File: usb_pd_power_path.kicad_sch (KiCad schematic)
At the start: 79 parts, among them Q10 Q_PMOS_DGS, Q11 Q_NMOS_DGS, Q12 Q_NMOS_DGS, Q13 Q_NMOS_DGS, Q14 Q_NMOS_DGS, Q15 Q_PMOS_DGS, Q16 Q_PMOS_DGS, Q17 Q_NMOS_DGS, Q18 Q_NMOS_DGS, Q9 Q_PMOS_DGS, U15 LM358, U16 MP2229GQ-P, U17 MP2229GQ-P

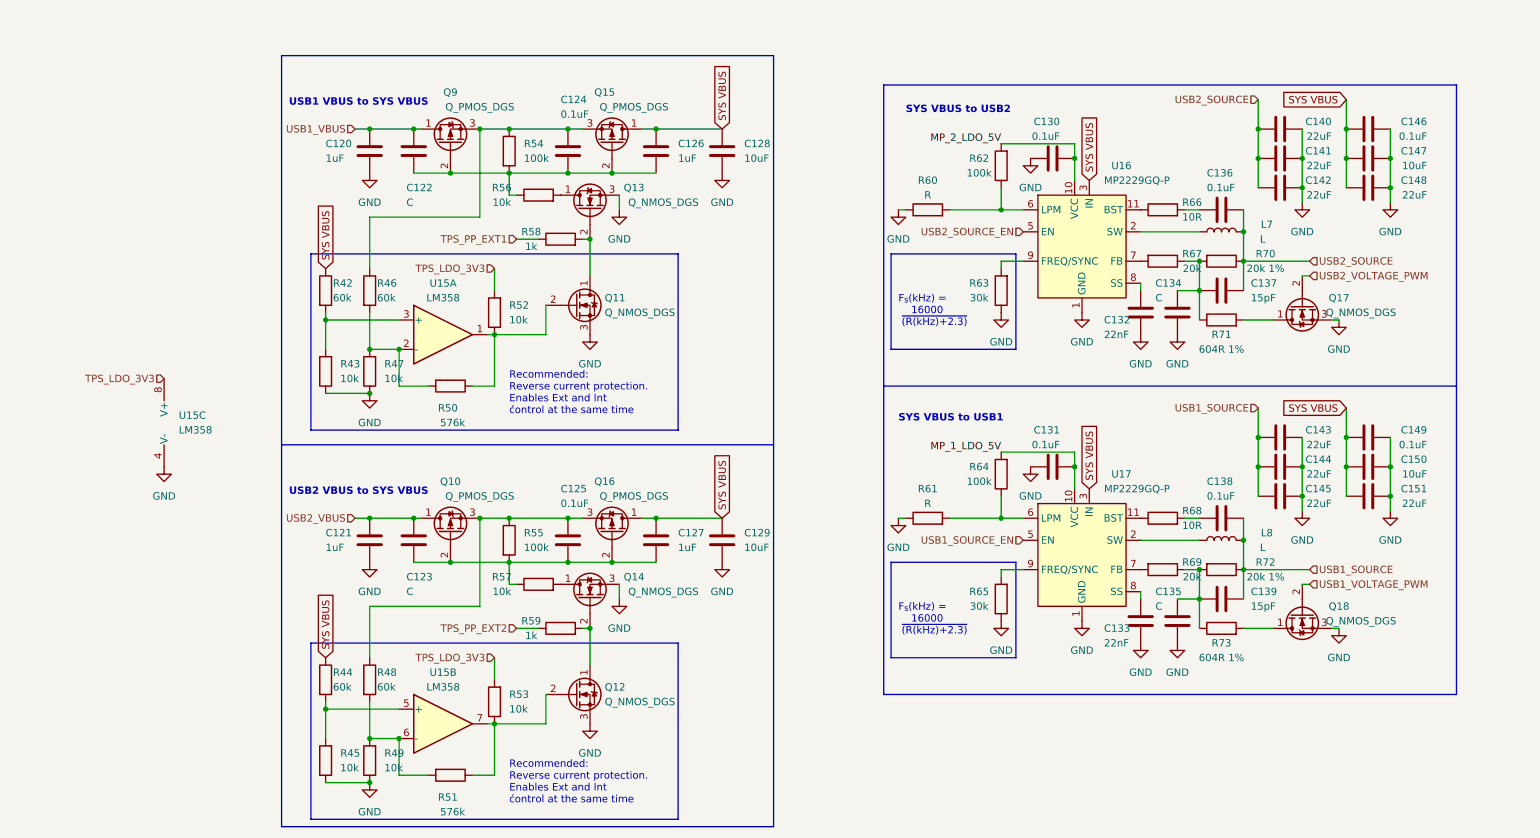
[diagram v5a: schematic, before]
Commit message: added nfc antenna components, added most of footprints
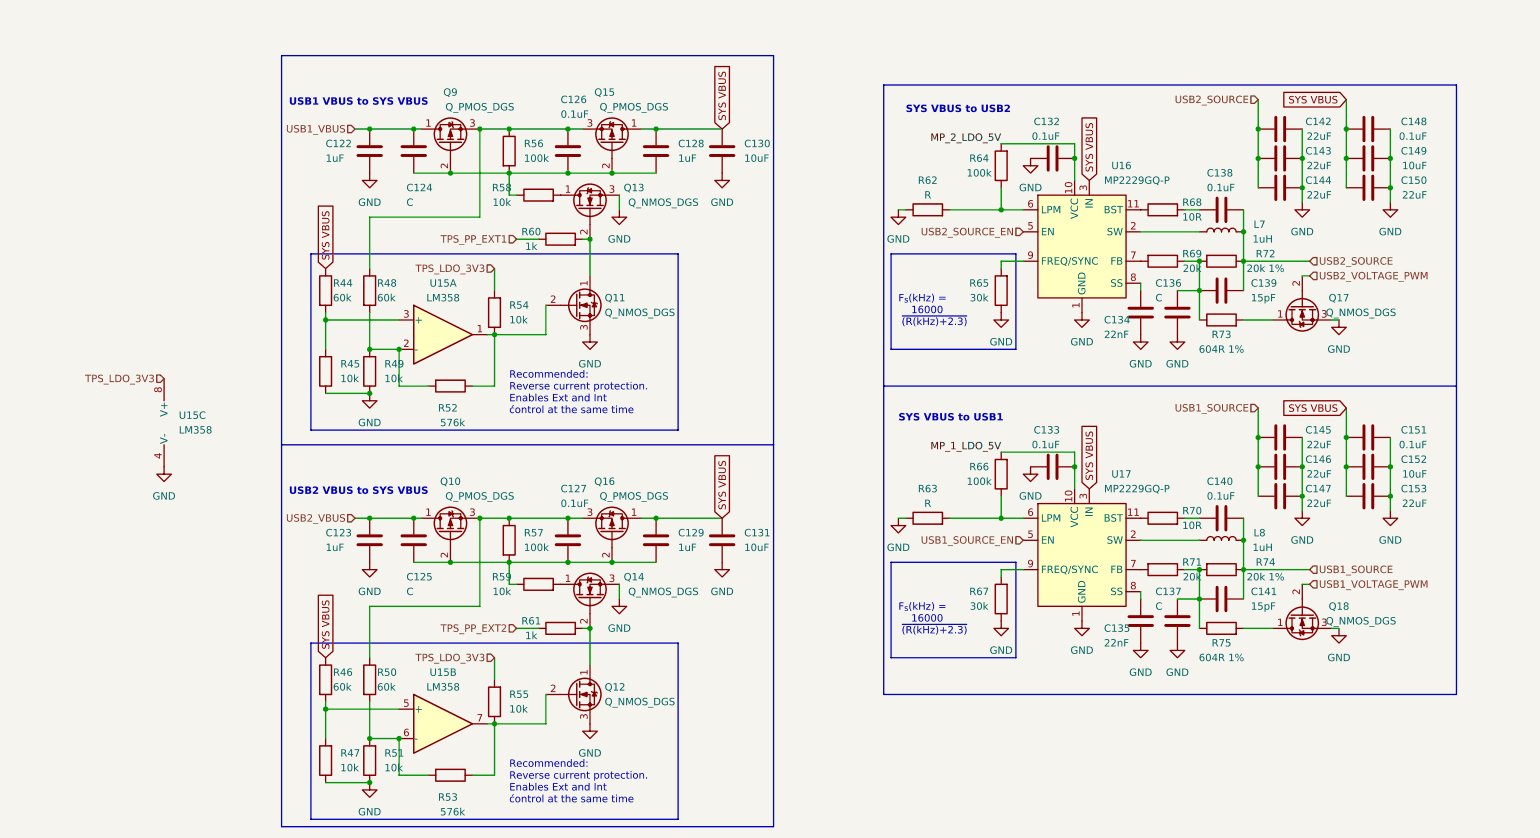
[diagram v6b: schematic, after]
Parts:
- C122: renamed from C120; footprint (none) -> Capacitor_SMD:C_0603_1608Metric_Pad1.08x0.95mm_HandSolder
- C123: renamed from C121; footprint (none) -> Capacitor_SMD:C_0603_1608Metric_Pad1.08x0.95mm_HandSolder
- C124: renamed from C122; footprint (none) -> Capacitor_SMD:C_0603_1608Metric_Pad1.08x0.95mm_HandSolder
- C125: renamed from C123; footprint (none) -> Capacitor_SMD:C_0603_1608Metric_Pad1.08x0.95mm_HandSolder
- C126: renamed from C124; footprint (none) -> Capacitor_SMD:C_0603_1608Metric_Pad1.08x0.95mm_HandSolder
- C127: renamed from C125; footprint (none) -> Capacitor_SMD:C_0603_1608Metric_Pad1.08x0.95mm_HandSolder
- C128: renamed from C126; footprint (none) -> Capacitor_SMD:C_0603_1608Metric_Pad1.08x0.95mm_HandSolder
- C129: renamed from C127; footprint (none) -> Capacitor_SMD:C_0603_1608Metric_Pad1.08x0.95mm_HandSolder
- C132: renamed from C130; footprint (none) -> Capacitor_SMD:C_0603_1608Metric_Pad1.08x0.95mm_HandSolder
- C133: renamed from C131; footprint (none) -> Capacitor_SMD:C_0603_1608Metric_Pad1.08x0.95mm_HandSolder
- C134: renamed from C132; footprint (none) -> Capacitor_SMD:C_0603_1608Metric_Pad1.08x0.95mm_HandSolder
- C135: renamed from C133; footprint (none) -> Capacitor_SMD:C_0603_1608Metric_Pad1.08x0.95mm_HandSolder
- C136: renamed from C134; footprint (none) -> Capacitor_SMD:C_0603_1608Metric_Pad1.08x0.95mm_HandSolder
- C137: renamed from C135; footprint (none) -> Capacitor_SMD:C_0603_1608Metric_Pad1.08x0.95mm_HandSolder
- C138: renamed from C136; footprint (none) -> Capacitor_SMD:C_0603_1608Metric_Pad1.08x0.95mm_HandSolder
- C139: renamed from C137; footprint (none) -> Capacitor_SMD:C_0603_1608Metric_Pad1.08x0.95mm_HandSolder
- C140: renamed from C138; footprint (none) -> Capacitor_SMD:C_0603_1608Metric_Pad1.08x0.95mm_HandSolder
- C141: renamed from C139; footprint (none) -> Capacitor_SMD:C_0603_1608Metric_Pad1.08x0.95mm_HandSolder
- C148: renamed from C146; footprint (none) -> Capacitor_SMD:C_0603_1608Metric_Pad1.08x0.95mm_HandSolder
- C151: renamed from C149; footprint (none) -> Capacitor_SMD:C_0603_1608Metric_Pad1.08x0.95mm_HandSolder
- L7, L8: value L -> 1uH
- R44: renamed from R42; footprint (none) -> Resistor_SMD:R_0603_1608Metric_Pad0.98x0.95mm_HandSolder
- R45: renamed from R43; footprint (none) -> Resistor_SMD:R_0603_1608Metric_Pad0.98x0.95mm_HandSolder
- R46: renamed from R44; footprint (none) -> Resistor_SMD:R_0603_1608Metric_Pad0.98x0.95mm_HandSolder
- R47: renamed from R45; footprint (none) -> Resistor_SMD:R_0603_1608Metric_Pad0.98x0.95mm_HandSolder
- R48: renamed from R46; footprint (none) -> Resistor_SMD:R_0603_1608Metric_Pad0.98x0.95mm_HandSolder
- R49: renamed from R47; footprint (none) -> Resistor_SMD:R_0603_1608Metric_Pad0.98x0.95mm_HandSolder
- R50: renamed from R48; footprint (none) -> Resistor_SMD:R_0603_1608Metric_Pad0.98x0.95mm_HandSolder
- R51: renamed from R49; footprint (none) -> Resistor_SMD:R_0603_1608Metric_Pad0.98x0.95mm_HandSolder
- R52: renamed from R50; footprint (none) -> Resistor_SMD:R_0603_1608Metric_Pad0.98x0.95mm_HandSolder
- R53: renamed from R51; footprint (none) -> Resistor_SMD:R_0603_1608Metric_Pad0.98x0.95mm_HandSolder
- R54: renamed from R52; footprint (none) -> Resistor_SMD:R_0603_1608Metric_Pad0.98x0.95mm_HandSolder
- R55: renamed from R53; footprint (none) -> Resistor_SMD:R_0603_1608Metric_Pad0.98x0.95mm_HandSolder
- R56: renamed from R54; footprint (none) -> Resistor_SMD:R_0603_1608Metric_Pad0.98x0.95mm_HandSolder
- R57: renamed from R55; footprint (none) -> Resistor_SMD:R_0603_1608Metric_Pad0.98x0.95mm_HandSolder
- R58: renamed from R56; footprint (none) -> Resistor_SMD:R_0603_1608Metric_Pad0.98x0.95mm_HandSolder
- R59: renamed from R57; footprint (none) -> Resistor_SMD:R_0603_1608Metric_Pad0.98x0.95mm_HandSolder
- R60: renamed from R58; footprint (none) -> Resistor_SMD:R_0603_1608Metric_Pad0.98x0.95mm_HandSolder
- R61: renamed from R59; footprint (none) -> Resistor_SMD:R_0603_1608Metric_Pad0.98x0.95mm_HandSolder
- R62: renamed from R60; footprint (none) -> Resistor_SMD:R_0603_1608Metric_Pad0.98x0.95mm_HandSolder
- R63: renamed from R61; footprint (none) -> Resistor_SMD:R_0603_1608Metric_Pad0.98x0.95mm_HandSolder
- R64: renamed from R62; footprint (none) -> Resistor_SMD:R_0603_1608Metric_Pad0.98x0.95mm_HandSolder
- R65: renamed from R63; footprint (none) -> Resistor_SMD:R_0603_1608Metric_Pad0.98x0.95mm_HandSolder
- R66: renamed from R64; footprint (none) -> Resistor_SMD:R_0603_1608Metric_Pad0.98x0.95mm_HandSolder
- R67: renamed from R65; footprint (none) -> Resistor_SMD:R_0603_1608Metric_Pad0.98x0.95mm_HandSolder
- R68: renamed from R66; footprint (none) -> Resistor_SMD:R_0603_1608Metric_Pad0.98x0.95mm_HandSolder
- R69: renamed from R67; footprint (none) -> Resistor_SMD:R_0603_1608Metric_Pad0.98x0.95mm_HandSolder
- R70: renamed from R68; footprint (none) -> Resistor_SMD:R_0603_1608Metric_Pad0.98x0.95mm_HandSolder
- R71: renamed from R69; footprint (none) -> Resistor_SMD:R_0603_1608Metric_Pad0.98x0.95mm_HandSolder
- R72: renamed from R70; footprint (none) -> Resistor_SMD:R_0603_1608Metric_Pad0.98x0.95mm_HandSolder
- R73: renamed from R71; footprint (none) -> Resistor_SMD:R_0603_1608Metric_Pad0.98x0.95mm_HandSolder
- R74: renamed from R72; footprint (none) -> Resistor_SMD:R_0603_1608Metric_Pad0.98x0.95mm_HandSolder
- R75: renamed from R73; footprint (none) -> Resistor_SMD:R_0603_1608Metric_Pad0.98x0.95mm_HandSolder
- U15: footprint (none) -> Package_SO:SOIC-8_3.9x4.9mm_P1.27mm
- U16, U17: footprint (none) -> airsoft_controller:QFN-14
- renumbered C128 to C130, C129 to C131, C140 to C142, C141 to C143, C142 to C144, C143 to C145, C144 to C146, C145 to C147, C147 to C149, C148 to C150, C150 to C152, C151 to C153

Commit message: schematic creation
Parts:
- removed Q10, Q15, Q16, Q9: Q_PMOS_DGS, symbol Device:Q_PMOS_DGS
- added Q10, Q9: Q_Dual_PMOS, Package_SO:SO-8_3.9x4.9mm_P1.27mm, symbol Device:Q_Dual_PMOS_S1G1S2G2D2D2D1D1
- added R63, R64: 100k, Resistor_SMD:R_0603_1608Metric_Pad0.98x0.95mm_HandSolder, symbol Device:R
- C132: renamed from C124; value C -> 0.1uF
- C133: renamed from C125; value C -> 0.1uF
- C136: renamed from C128; value 1uF -> 0.1uF
- C137: renamed from C129; value 1uF -> 0.1uF
- C138: renamed from C130; footprint (none) -> Capacitor_SMD:C_0805_2012Metric_Pad1.18x1.45mm_HandSolder
- C139: renamed from C131; footprint (none) -> Capacitor_SMD:C_0805_2012Metric_Pad1.18x1.45mm_HandSolder
- C150: renamed from C142; footprint (none) -> Capacitor_SMD:CP_Elec_5x5.3; symbol Device:C -> Device:C_Polarized
- C151: renamed from C143; footprint (none) -> Capacitor_SMD:CP_Elec_5x5.3; symbol Device:C -> Device:C_Polarized
- C152: renamed from C144; footprint (none) -> Capacitor_SMD:CP_Elec_5x5.3; symbol Device:C -> Device:C_Polarized
- C153: renamed from C145; footprint (none) -> Capacitor_SMD:CP_Elec_5x5.3; symbol Device:C -> Device:C_Polarized
- C154: renamed from C146; footprint (none) -> Capacitor_SMD:CP_Elec_5x5.3; symbol Device:C -> Device:C_Polarized
- C155: renamed from C147; footprint (none) -> Capacitor_SMD:CP_Elec_5x5.3; symbol Device:C -> Device:C_Polarized
- C157: renamed from C149; footprint (none) -> Capacitor_SMD:C_1206_3216Metric_Pad1.33x1.80mm_HandSolder
- C158: renamed from C150; footprint (none) -> Capacitor_SMD:CP_Elec_5x5.3; symbol Device:C -> Device:C_Polarized
- C160: renamed from C152; footprint (none) -> Capacitor_SMD:C_1206_3216Metric_Pad1.33x1.80mm_HandSolder
- C161: renamed from C153; footprint (none) -> Capacitor_SMD:CP_Elec_5x5.3; symbol Device:C -> Device:C_Polarized
- L7, L8: footprint (none) -> airsoft_controller:Inductor_8030
- Q11, Q12, Q13, Q14: footprint (none) -> Package_TO_SOT_SMD:SOT-23; symbol Device:Q_NMOS_DGS -> Device:Q_NMOS_GSD
- Q15: renamed from Q17; footprint (none) -> Package_TO_SOT_SMD:SOT-23; symbol Device:Q_NMOS_DGS -> Device:Q_NMOS_GSD
- Q16: renamed from Q18; footprint (none) -> Package_TO_SOT_SMD:SOT-23; symbol Device:Q_NMOS_DGS -> Device:Q_NMOS_GSD
- renumbered C122 to C130, C123 to C131, C126 to C134, C127 to C135, C132 to C140, C133 to C141, C134 to C142, C135 to C143, C136 to C144, C137 to C145, C138 to C146, C139 to C147, C140 to C148, C141 to C149, C148 to C156, C151 to C159, R44 to R45, R45 to R46, R46 to R47, R47 to R48, R48 to R49, R49 to R50, R50 to R51, R51 to R52, R52 to R53, R53 to R54, R54 to R55, R55 to R56, R56 to R57, R57 to R58, R58 to R59, R59 to R60, R60 to R61, R61 to R62, R62 to R65, R63 to R66, R64 to R67, R65 to R68, R66 to R69, R67 to R70, R68 to R71, R69 to R72, R70 to R73, R71 to R74, R72 to R75, R73 to R76, R74 to R77, R75 to R78, U15 to U17, U16 to U18, U17 to U19
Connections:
- net GND: now also Q11.2 (S), Q12.2 (S), Q13.2 (S), Q14.2 (S), Q15.2 (S), Q16.2 (S), R63.2, R64.2; no longer Q11.3 (S), Q12.3 (S), Q13.3 (S), Q14.3 (S), Q15.3 (S), Q16.3 (S)
- net SYS VBUS: now also U18.15 (IN), U19.15 (IN), Q10.5 (D), Q10.6 (G), Q9.5 (D), Q9.6 (G); no longer U18.PAD (IN), U19.PAD (IN)
- net USB1_VBUS: now also Q9.7 (D), Q9.8 (G)
- net USB1_VOLTAGE_PWM: now also Q16.1 (G); no longer Q16.2 (G)
- net USB2_VBUS: now also Q10.7 (D), Q10.8 (G)
- net USB2_VOLTAGE_PWM: now also Q15.1 (G); no longer Q15.2 (G)
- net at R76.2: now also Q15.3 (D); no longer Q15.1 (D)
- net at C133.2, C135.2, C137.2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: now also Q10.2 (G), Q10.4 (G)
- net at R53.1, R55.1, U17.1: now also Q11.1 (G); no longer Q11.2 (G)
- net at R60.2: now also Q14.3 (D); no longer Q14.1 (D)
- net at C132.2, C134.2, C136.2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: now also Q9.2 (G), Q9.4 (G)
- net at Q13.1 (G): now also Q11.3 (D), R61.2, R63.1; no longer R59.2
- net at C134.1, R49.1, R57.1: now also Q9.1 (S), Q9.3 (S)
- net at C135.1, R51.1, R58.1: now also Q10.1 (S), Q10.3 (S)
- net at R54.1, R56.1, U17.7: now also Q12.1 (G); no longer Q12.2 (G)
- net at R78.2: now also Q16.3 (D); no longer Q16.1 (D)
- new net: Q13.3 (D), R59.2
- new net: Q12.3 (D), Q14.1 (G), R62.2, R64.1
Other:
- moved on the sheet: C141, C143, C145, C148, C149, C159, C160, L8, Q15, Q16, R66, R69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

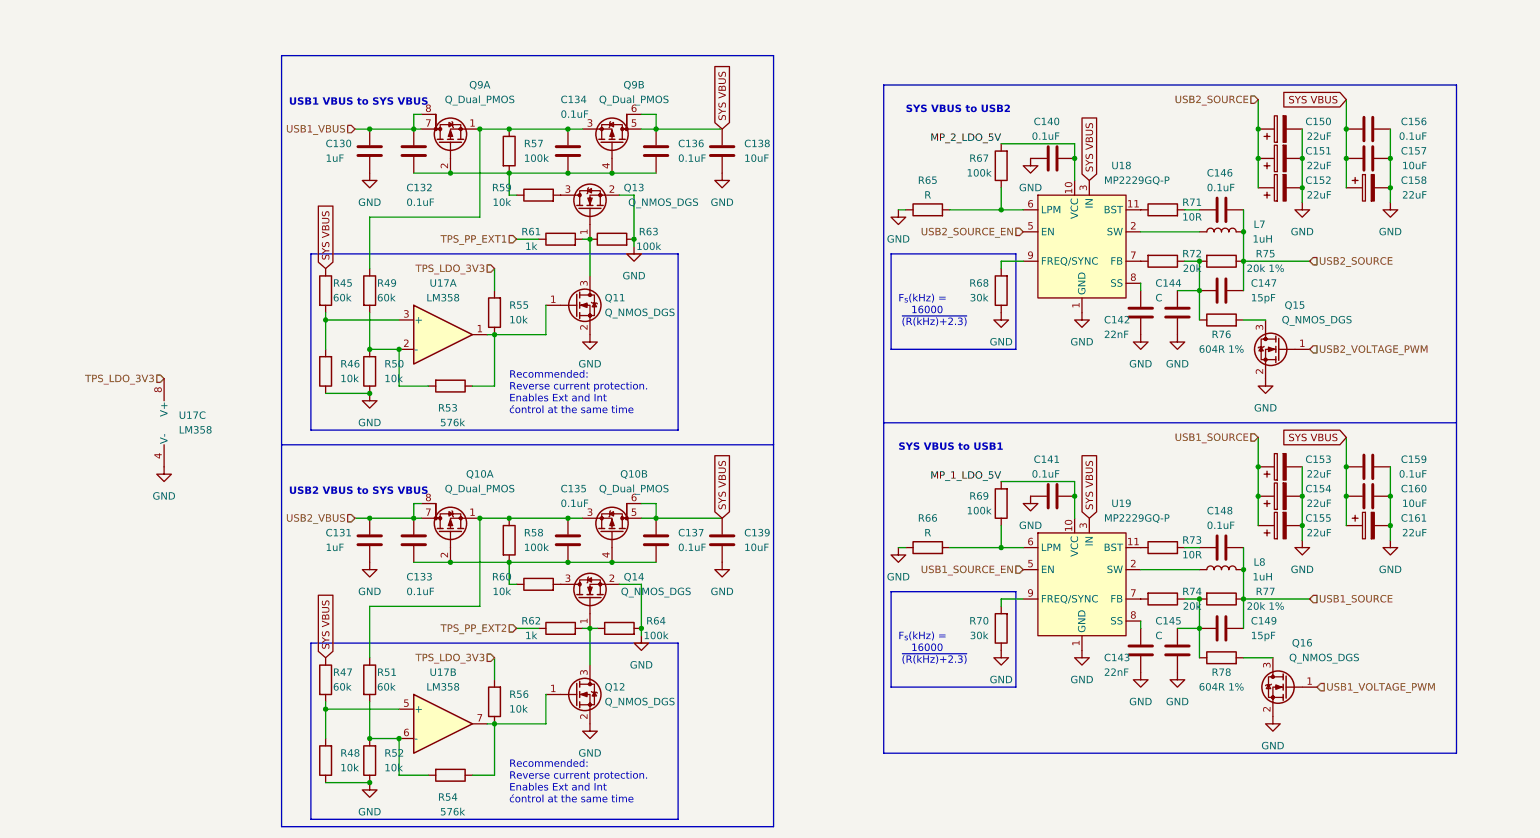
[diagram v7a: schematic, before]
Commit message: usb power source added, need to reassemble to 4-layers
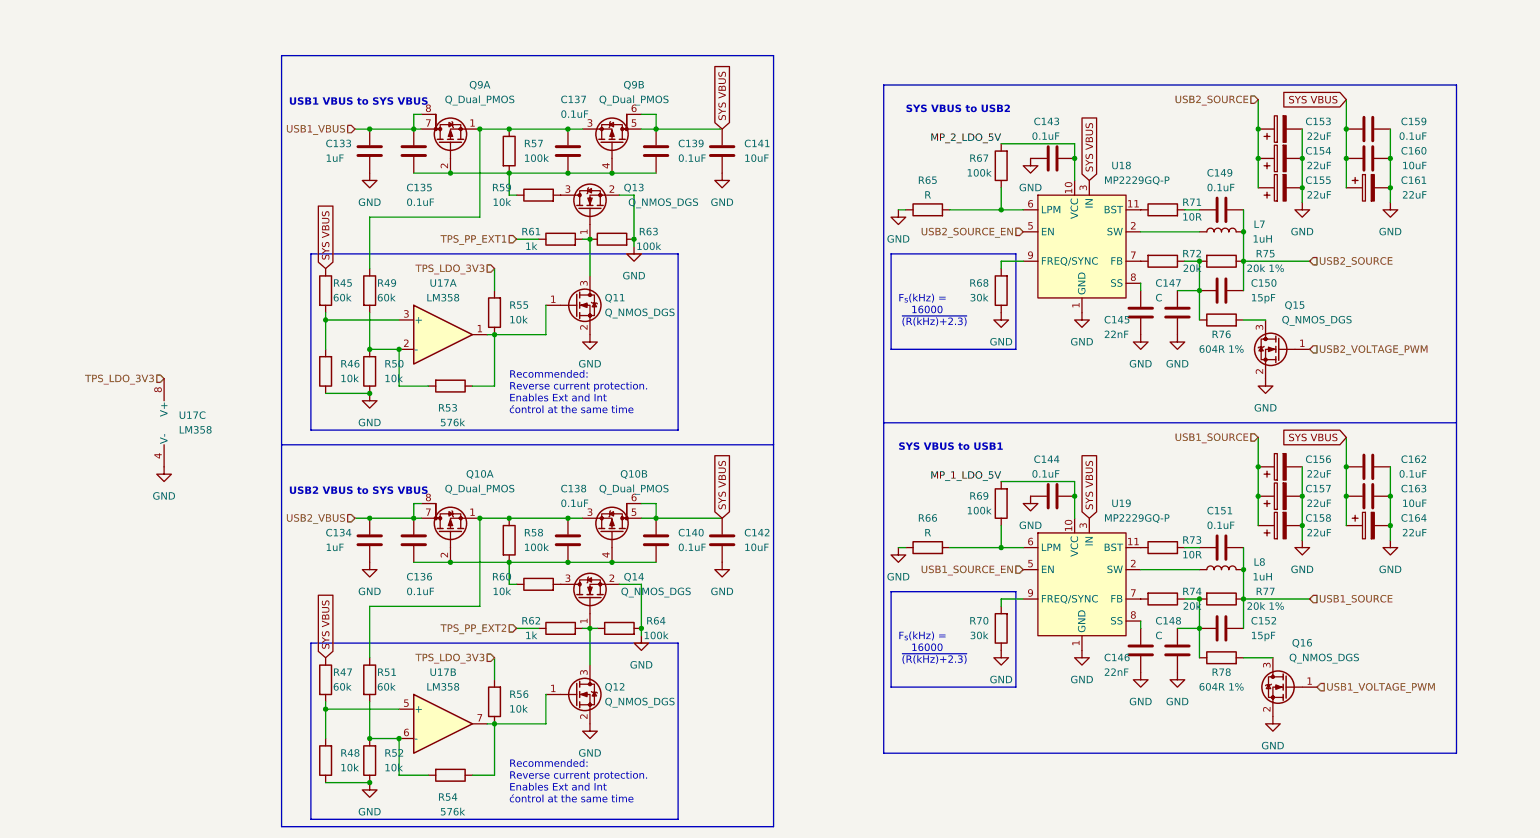
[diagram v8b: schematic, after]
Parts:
- C160: renamed from C157; footprint Capacitor_SMD:C_1206_3216Metric_Pad1.33x1.80mm_HandSolder -> Capacitor_SMD:C_0805_2012Metric_Pad1.18x1.45mm_HandSolder
- C163: renamed from C160; footprint Capacitor_SMD:C_1206_3216Metric_Pad1.33x1.80mm_HandSolder -> Capacitor_SMD:C_0805_2012Metric_Pad1.18x1.45mm_HandSolder
- renumbered C130 to C133, C131 to C134, C132 to C135, C133 to C136, C134 to C137, C135 to C138, C136 to C139, C137 to C140, C138 to C141, C139 to C142, C140 to C143, C141 to C144, C142 to C145, C143 to C146, C144 to C147, C145 to C148, C146 to C149, C147 to C150, C148 to C151, C149 to C152, C150 to C153, C151 to C154, C152 to C155, C153 to C156, C154 to C157, C155 to C158, C156 to C159, C158 to C161, C159 to C162, C161 to C164
